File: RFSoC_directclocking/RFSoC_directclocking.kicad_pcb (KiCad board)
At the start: 2 copper layers, 54.6 x 43.2 mm, 16 parts, among them U1 TCM2-33WX+, U2 TCM2-33WX+

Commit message: mc lib components
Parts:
- moved clk-in 43.0 mm to (128.0, 79.1), turned to 0 degrees
- moved C1 23.4 mm to (118.1, 79.1), turned to 180 degrees
- moved clkb+ 17.8 mm to (79.0, 94.0)
- moved clka+ 11.9 mm to (84.1, 60.9)
- moved clkb- 9.54 mm to (116.4, 94.0)
- moved clka- 8.18 mm to (116.3, 61.1)
- moved C2 4.82 mm to (92.4, 86.1), turned to 180 degrees
- moved C4 4.50 mm to (95.7, 72.2), turned to 180 degrees
- moved R1 3.24 mm to (100.8, 78.6), turned to 180 degrees
- moved R2 3.24 mm to (100.8, 79.6), turned to 180 degrees
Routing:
- net Net-(C1-Pad2): track 4.00 -> 18.2 mm
- net Net-(C3-Pad2): track 30.4 -> 19.4 mm
- net Net-(C2-Pad2): track 9.14 -> 19.5 mm
- net Net-(C4-Pad2): track 9.68 -> 18.9 mm
- net Net-(C5-Pad2): track 26.0 -> 18.9 mm
- net Net-(C4-Pad1): track 2.16 -> 3.17 mm
- net Net-(C2-Pad1): track 2.60 -> 3.23 mm
- net GND: vias 66 -> 0
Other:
- board size 54.6 x 43.2 mm -> 57.2 x 38.1 mm

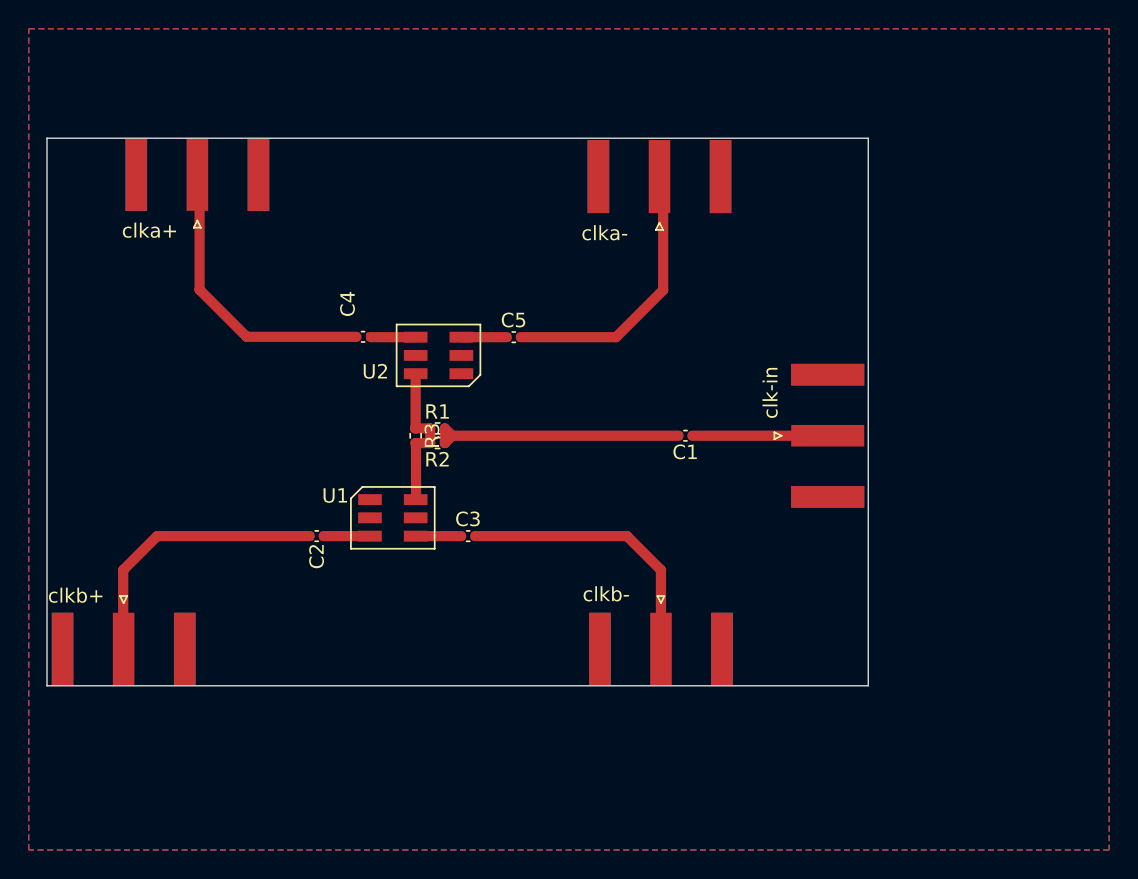
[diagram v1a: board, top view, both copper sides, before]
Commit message: Squashed commit of the following:
commit 11c362fd04afcdda8fc54016fc262973d8ee90dd
Author: cody <you@example.com>
Date:   Sat May 14 20:18:42 2022 -0700

    updated silkscreens, degin DRC corrections

commit c03c76887280f84603892cf274eefb7fb13b0fa8
Author: cody <you@example.com>
Date:   Fri May 13 16:10:57 2022 -0700

    fork em

commit e1673cb11a9ebe940ceda00a5b2ec080c415b465
Author: cody <you@example.com>
Date:   Fri May 13 15:38:00 2022 -0700

    updated all

commit 84fbdba19d4f5d8a85804f2c5d387b833a8e7f5e
Author: Cody Roberson <carobers@asu.edu>
Date:   Mon May 9 16:15:14 2022 -0700

    Finished Updated ADC schematic

    ADC schematic was modified to match the pin map between
    the rfsoc and the xm500.

commit 1e4de3bc2e504d4b0d3d294a2c6c5a2a5a485041
Author: cody <you@example.com>
Date:   Mon May 9 10:21:30 2022 -0700

    progress check

    Started Labeling process

commit 6cadb2acb3bb1a794e84b73e4dfc828af985fa6c
Author: cody <you@example.com>
Date:   Thu May 5 15:24:15 2022 -0700

    partial update of labels

commit 2dab10b1dfa9c61606f5d562ab6e543ae0948647
Merge: 76ba8d6 79e9342
Author: Cody Roberson <codyaroberson@outlook.com>
Date:   Wed Mar 9 20:07:10 2022 -0700

    Merge pull request #1 from CodyRoberson/twochannel_clk

    Twochannel clk

commit 79e93425439f23e00c2b0d92e892590d87fe78f7
Author: Cody Roberson <carobers@asu.edu>
Date:   Wed Mar 9 20:04:09 2022 -0700

    moved forkem and labeled ports

commit 9a4b6dc66818e11f3bb9969be501559d1f9e476d
Author: Cody Roberson <carobers@asu.edu>
Date:   Wed Mar 9 16:28:24 2022 -0700

    improvements

    Made improvement to kicad symbol and replaced footprint for baluns. They
    were incorrectly orientated with regards to pin numbering

commit 8d29e46f6a613ffa86cae2f2a7a070122b97e7eb
Author: Cody Roberson <carobers@asu.edu>
Date:   Wed Mar 9 14:50:01 2022 -0700

    added kicad symbol+footprint

commit 3c7e1566d05959f7dad261469b2e27b92f79ed87
Author: Cody Roberson <carobers@asu.edu>
Date:   Wed Mar 9 14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
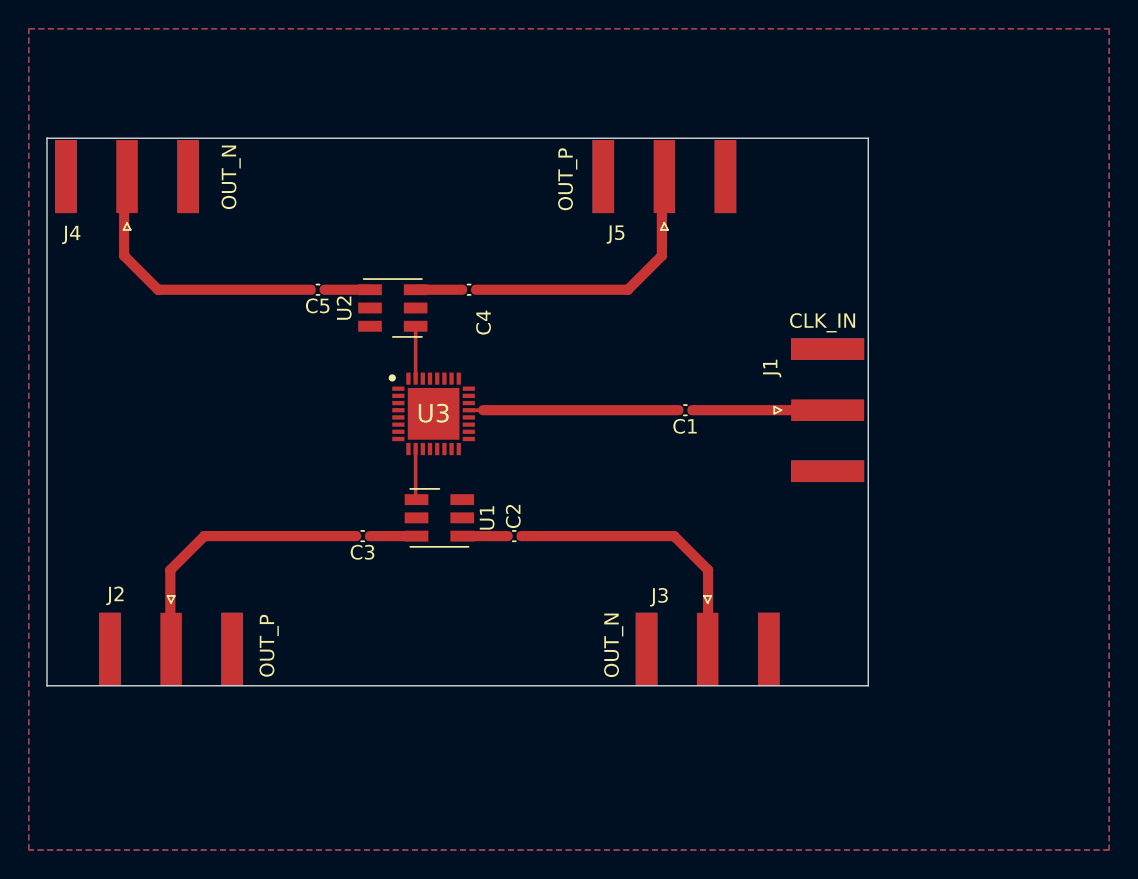
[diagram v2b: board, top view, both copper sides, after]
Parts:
- removed R1, R2: 50, Resistor_SMD:R_0402_1005Metric
- removed R3: 100, Resistor_SMD:R_0402_1005Metric
- added U3: EP2RCW+, Mouser:QFN50P500X500X100-33N-D, F.Cu at (100.6, 77.6)
- U1, U2: value TCM2-33WX+ -> Mini-Circuits_DB1627; footprint RF_Mini-Circuits:TCM2-33WX+ -> RF_Mini-Circuits:Mini-Circuits_DB1627
- moved G*** 46.6 mm to (84.9, 77.8)
- moved J3 40.6 mm to (119.6, 94.0)
- moved J4 37.0 mm to (79.2, 61.1)
- moved J2 34.1 mm to (82.3, 94.0)
- moved J5 32.5 mm to (116.6, 61.1)
- moved C5 14.0 mm to (92.5, 69.0), turned to 180 degrees
- moved C2 13.7 mm to (106.2, 86.1), turned to 0 degrees
- moved C4 8.07 mm to (103.0, 69.0), turned to 0 degrees
- moved C3 7.34 mm to (95.6, 86.1), turned to 180 degrees
- moved U2 4.58 mm to (97.7, 70.2)
- moved U1 3.24 mm to (101.0, 84.8)
- moved C1 1.78 mm to (118.1, 77.3)
- moved J1 1.78 mm to (128.0, 77.3)
- renumbered clk-in to J1, clkb- to J2, clkb+ to J3, clka- to J4, clka+ to J5
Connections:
- U1 pad 6: Net-(R2-Pad2) -> Net-(U1-Pad6)
- U2 pad 6: Net-(R2-Pad2) -> Net-(U2-Pad6)
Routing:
- net Net-(R2-Pad2): track 10.7 -> 0.00 mm
- net Net-(C1-Pad2): track 18.2 -> 14.4 mm
- net Net-(U2-Pad6): track 0.00 -> 3.65 mm
- net Net-(U1-Pad6): track 0.00 -> 3.55 mm
- net Net-(C5-Pad2): track 18.9 -> 19.5 mm
- net Net-(C4-Pad2): track 18.9 -> 19.4 mm
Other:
- board text added: "CLK_IN"
- board text added: "OUT_N"
- board text added: "OUT_P"
